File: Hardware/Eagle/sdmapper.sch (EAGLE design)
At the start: 32 parts, among them IC1 AM29F010J, IC2 HM628512ASOP32, IC3 XC95144XL_TQ100, IC4 LM1117-3V3, T1 BC858, T2 BC858, X1 50MHz

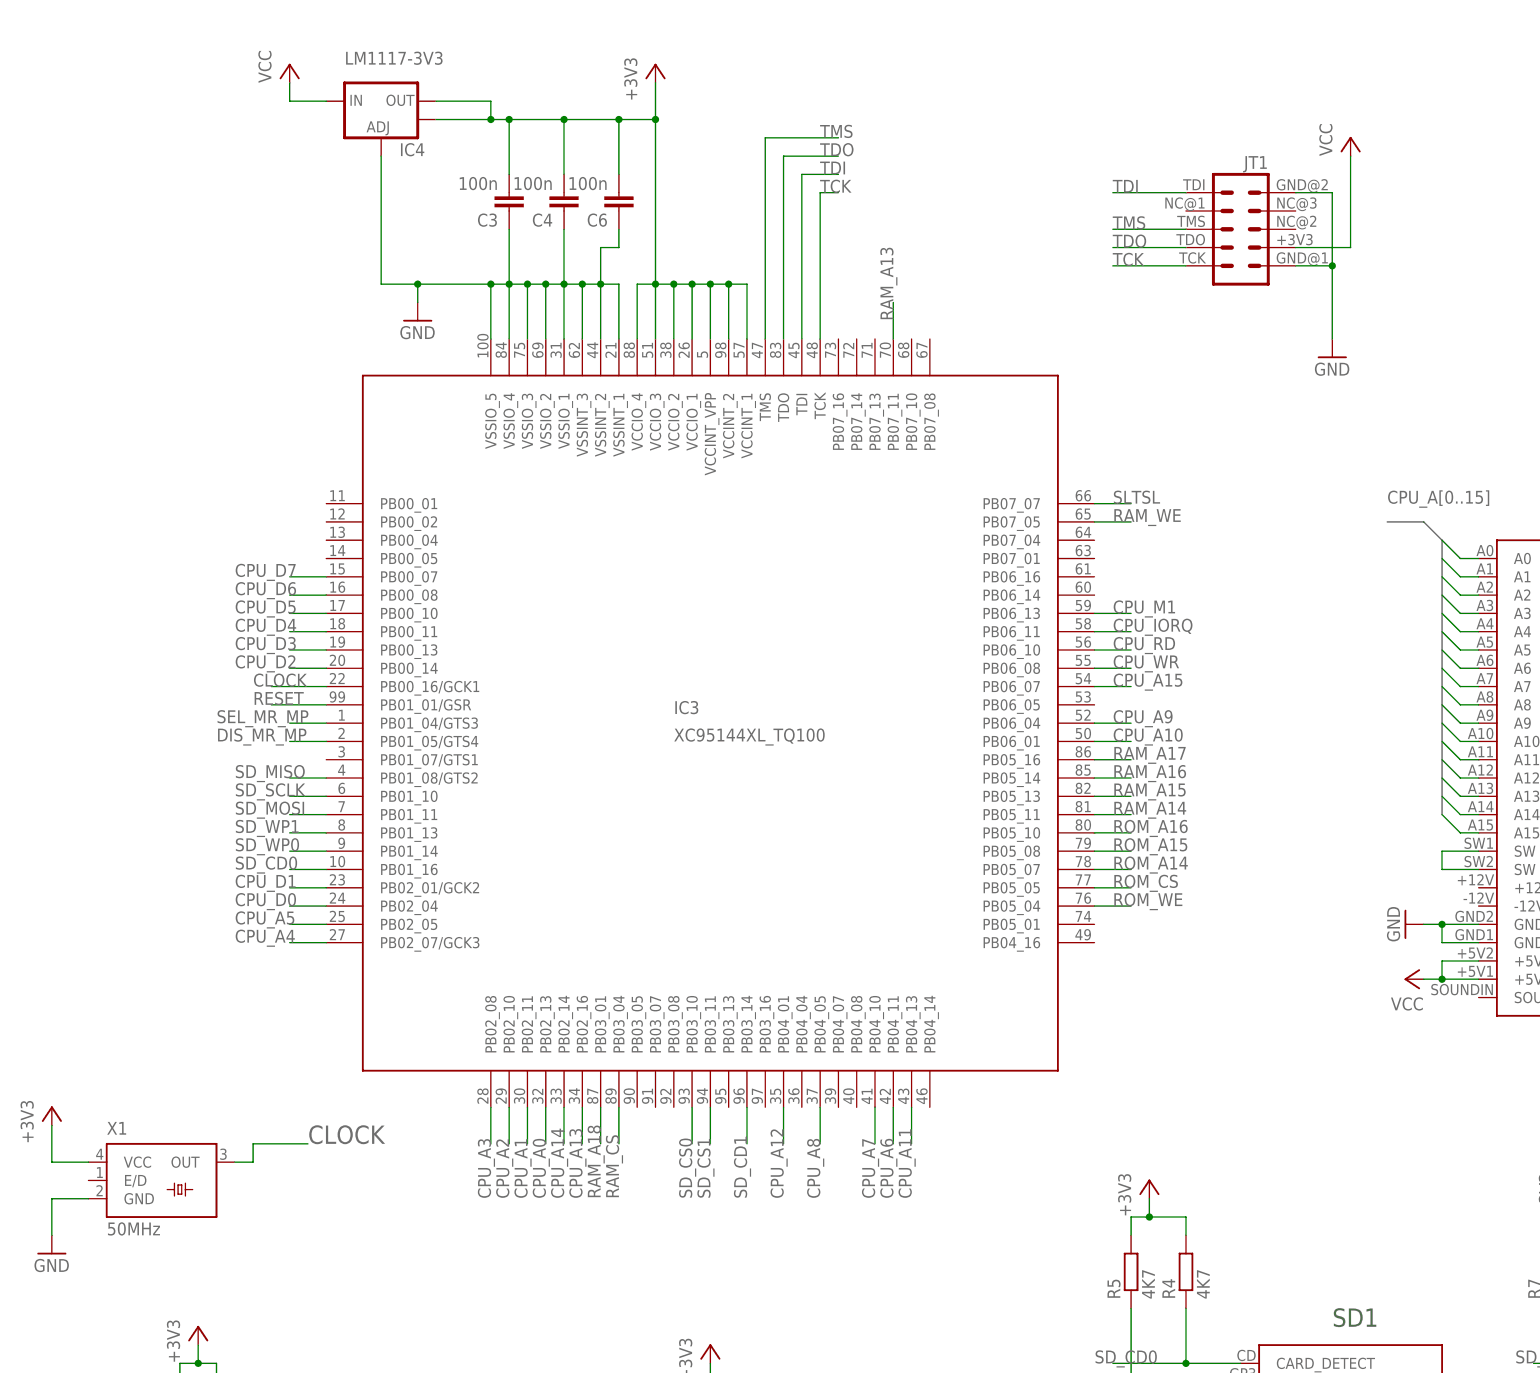
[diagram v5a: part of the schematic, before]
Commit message: Adicionado arquivos de gravação do CPLD nos formatos STAPL e SVF. Adicionado versão do driver em binário com patch para funcionar nas máquinas CIEL 2+. Corrigido BUG na placa onde o pino 1 da flash fica aterrada causando problemas com alguns modelos de flash que utilizam o sinal /RESET neste pino. Adicionado mais informações no silk da placa. Corrigido BUG de identificação da flash AM29F010 no atualizador.
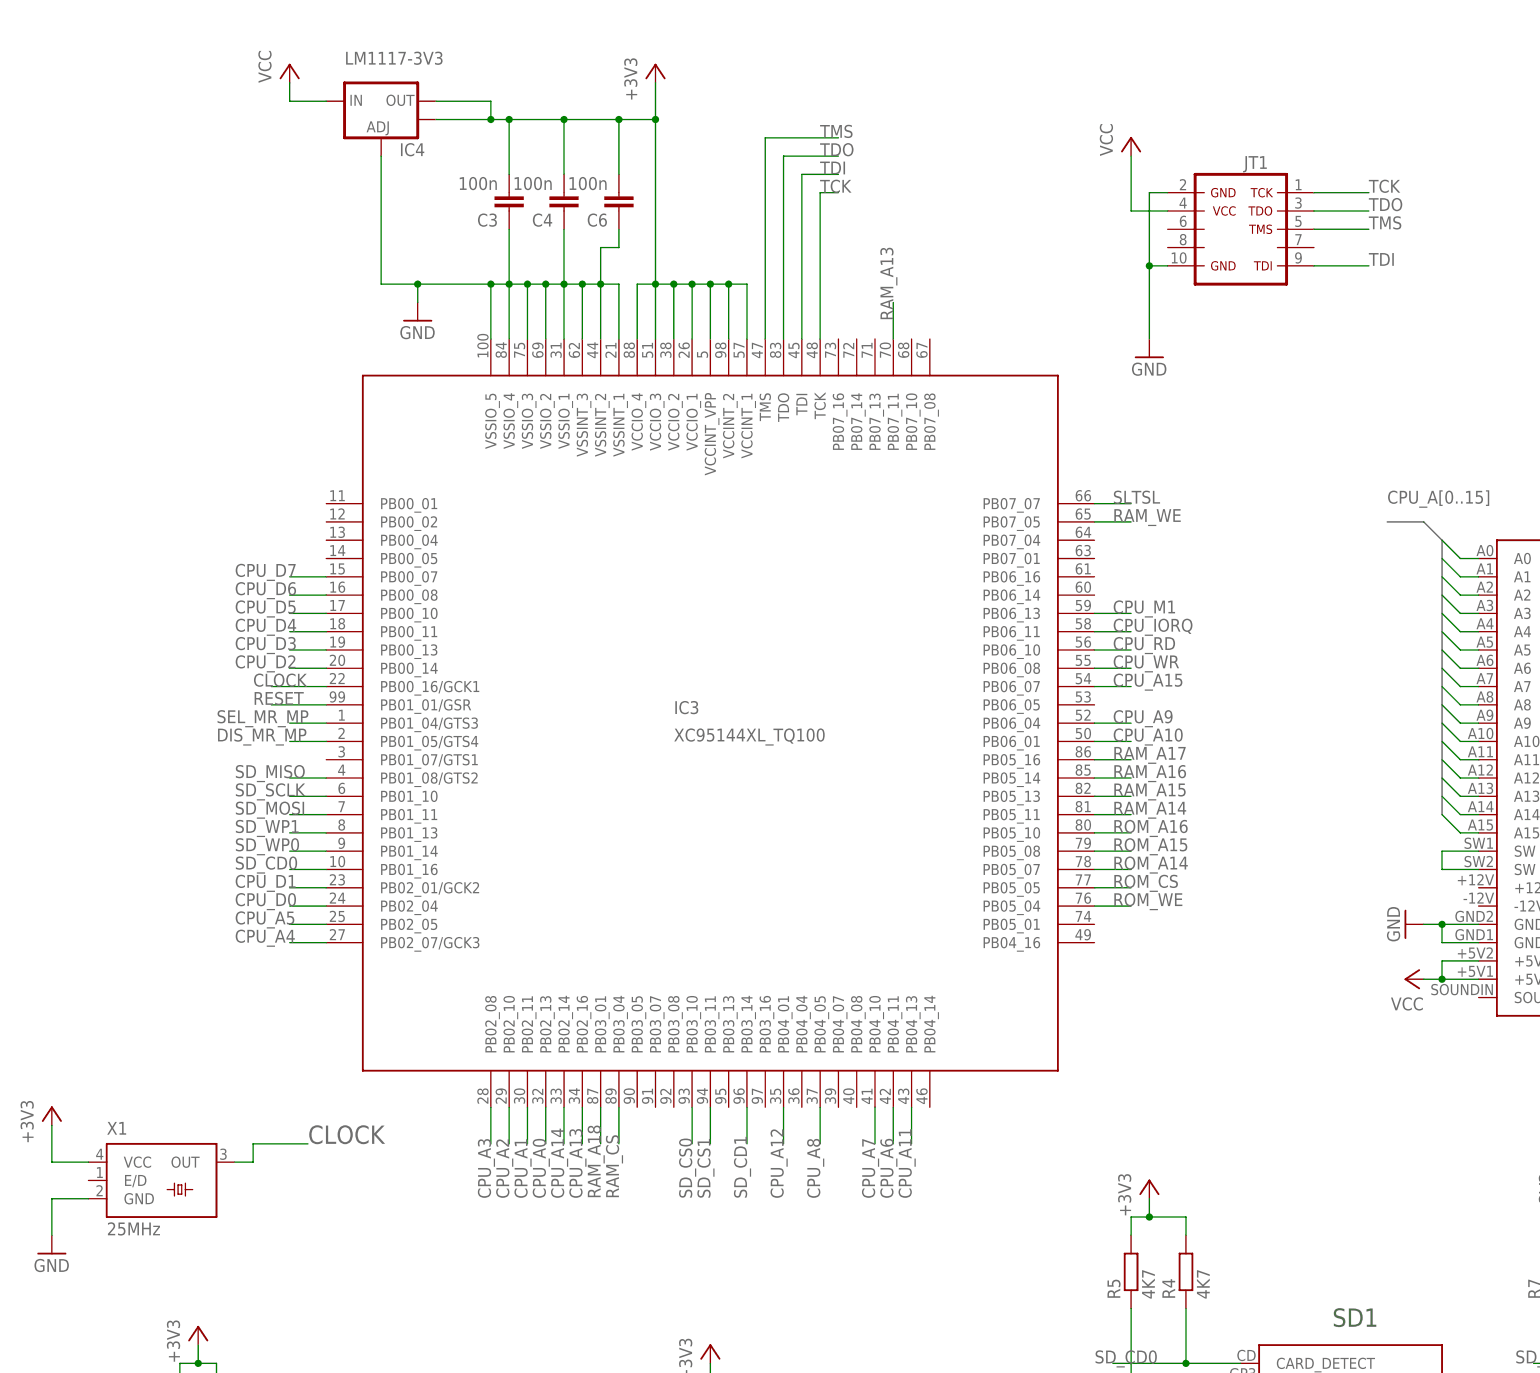
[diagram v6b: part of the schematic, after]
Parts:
- X1: value 50MHz -> 25MHz
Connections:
- net GND: now also JT1.10, JT1.2; no longer JT1.TCK, JT1.TDI
- net TCK: now also JT1.1; no longer JT1.GND@2
- net TDI: now also JT1.9; no longer JT1.GND@1
- net TDO: now also JT1.3; no longer JT1.NC@3
- net TMS: now also JT1.5; no longer JT1.NC@2
- net VCC: now also JT1.4; no longer JT1.NC@1
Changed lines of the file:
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@@
 <setting verticaltext="up"/>
 </settings>
-<grid distance="0.1" unitdist="inch" unit="inch" style="lines" multiple="1" display="no" altdistance="0.01" altunitdist="inch" altunit="inch"/>
+<grid distance="0.1" unitdist="inch" unit="mil" style="lines" multiple="1" display="no" altdistance="0.01" altunitdist="inch" altunit="inch"/>
 <layers>
 <layer number="1" name="Top" color="4" fill="1" visible="yes" active="no"/>
@@
 <part name="+3V9" library="supply1" deviceset="+3V3" device=""/>
 <part name="GND10" library="supply1" deviceset="GND" device=""/>
-<part name="X1" library="crystal" deviceset="SM77H" device="" value="50MHz"/>
+<part name="X1" library="crystal" deviceset="SM77H" device="" value="25MHz"/>
 </parts>
 <sheets>
@@
 <instance part="C4" gate="G$1" x="88.9" y="228.6" rot="R180"/>
 <instance part="GND7" gate="1" x="20.32" y="17.78"/>
-<instance part="GND32" gate="1" x="195.58" y="208.28"/>
-<instance part="P+24" gate="VCC" x="198.12" y="238.76"/>
+<instance part="GND32" gate="1" x="170.18" y="208.28"/>
+<instance part="P+24" gate="VCC" x="167.64" y="238.76"/>
 <instance part="R4" gate="G$1" x="175.26" y="81.28" rot="R90"/>
 <instance part="R5" gate="G$1" x="167.64" y="81.28" rot="R90"/>
@@
 <segment>
 <pinref part="P+24" gate="VCC" pin="VCC"/>
-<wire x1="190.5" y1="223.52" x2="198.12" y2="223.52" width="0.1524" layer="91"/>
-<wire x1="198.12" y1="223.52" x2="198.12" y2="236.22" width="0.1524" layer="91"/>
-<pinref part="JT1" gate="G$1" pin="NC@1"/>
+<wire x1="167.64" y1="228.6" x2="167.64" y2="236.22" width="0.1524" layer="91"/>
+<pinref part="JT1" gate="G$1" pin="4"/>
+<wire x1="172.72" y1="228.6" x2="167.64" y2="228.6" width="0.1524" layer="91"/>
 </segment>
 </net>
@@
 </segment>
 <segment>
-<wire x1="190.5" y1="220.98" x2="195.58" y2="220.98" width="0.1524" layer="91"/>
-<wire x1="195.58" y1="220.98" x2="195.58" y2="210.82" width="0.1524" layer="91"/>
 <pinref part="GND32" gate="1" pin="GND"/>
-<wire x1="190.5" y1="231.14" x2="195.58" y2="231.14" width="0.1524" layer="91"/>
-<wire x1="195.58" y1="231.14" x2="195.58" y2="220.98" width="0.1524" layer="91"/>
-<junction x="195.58" y="220.98"/>
-<pinref part="JT1" gate="G$1" pin="TDI"/>
-<pinref part="JT1" gate="G$1" pin="TCK"/>
+<wire x1="170.18" y1="231.14" x2="170.18" y2="220.98" width="0.1524" layer="91"/>
+<pinref part="JT1" gate="G$1" pin="2"/>
+<wire x1="170.18" y1="220.98" x2="170.18" y2="210.82" width="0.1524" layer="91"/>
+<wire x1="170.18" y1="231.14" x2="172.72" y2="231.14" width="0.1524" layer="91"/>
+<pinref part="JT1" gate="G$1" pin="10"/>
+<wire x1="172.72" y1="220.98" x2="170.18" y2="220.98" width="0.1524" layer="91"/>
+<junction x="170.18" y="220.98"/>
 </segment>
 <segment>
@@
 </segment>
 <segment>
-<wire x1="165.1" y1="226.06" x2="175.26" y2="226.06" width="0.1524" layer="91"/>
-<label x="165.1" y="226.06" size="1.778" layer="95"/>
-<pinref part="JT1" gate="G$1" pin="NC@2"/>
+<pinref part="JT1" gate="G$1" pin="5"/>
+<wire x1="200.66" y1="226.06" x2="193.04" y2="226.06" width="0.1524" layer="91"/>
+<label x="200.66" y="226.06" size="1.778" layer="95" ratio="10"/>
 </segment>
 </net>
@@
 </segment>
 <segment>
-<wire x1="165.1" y1="231.14" x2="175.26" y2="231.14" width="0.1524" layer="91"/>
-<label x="165.1" y="231.14" size="1.778" layer="95"/>
-<pinref part="JT1" gate="G$1" pin="GND@1"/>
+<pinref part="JT1" gate="G$1" pin="9"/>
+<wire x1="200.66" y1="220.98" x2="193.04" y2="220.98" width="0.1524" layer="91"/>
+<label x="200.66" y="220.98" size="1.778" layer="95" ratio="10"/>
 </segment>
 </net>
@@
 </segment>
 <segment>
-<wire x1="165.1" y1="220.98" x2="175.26" y2="220.98" width="0.1524" layer="91"/>
-<label x="165.1" y="220.98" size="1.778" layer="95"/>
-<pinref part="JT1" gate="G$1" pin="GND@2"/>
+<pinref part="JT1" gate="G$1" pin="1"/>
+<wire x1="200.66" y1="231.14" x2="193.04" y2="231.14" width="0.1524" layer="91"/>
+<label x="200.66" y="231.14" size="1.778" layer="95" ratio="10"/>
 </segment>
 </net>
@@
 <net name="TDO" class="0">
 <segment>
-<wire x1="165.1" y1="223.52" x2="175.26" y2="223.52" width="0.1524" layer="91"/>
-<label x="165.1" y="223.52" size="1.778" layer="95"/>
-<pinref part="JT1" gate="G$1" pin="NC@3"/>
-</segment>
-<segment>
 <wire x1="119.38" y1="210.82" x2="119.38" y2="236.22" width="0.1524" layer="91"/>
 <wire x1="127" y1="236.22" x2="119.38" y2="236.22" width="0.1524" layer="91"/>
@@
 <pinref part="IC3" gate="G$1" pin="TDO"/>
 </segment>
-</net>
+<segment>
+<pinref part="JT1" gate="G$1" pin="3"/>
+<wire x1="200.66" y1="228.6" x2="193.04" y2="228.6" width="0.1524" layer="91"/>
+<label x="200.66" y="228.6" size="1.778" layer="95" ratio="10"/>
+</segment>
+</net>
